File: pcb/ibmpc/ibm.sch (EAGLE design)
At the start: 23 parts, among them J2 ATX24RH

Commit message: working on ibmpc
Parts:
- removed JP3: (no value), appleii:4PIN_FAN
- added JP1: (no value), appleii:4PIN_FAN
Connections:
- net +12V: now also JP1.1_GND; no longer JP3.2_VCC
- net GND: now also JP1.2_VCC; no longer JP3.1_GND
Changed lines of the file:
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@@
 <part name="U$2" library="atx_power_control" deviceset="CAR_FUSE_HOLDER" device="3IN1"/>
 <part name="P+3" library="supply1" library_urn="urn:adsk.eagle:library:371" deviceset="+5V" device=""/>
-<part name="P+5" library="supply1" library_urn="urn:adsk.eagle:library:371" deviceset="+12V" device=""/>
 <part name="J2" library="macse" deviceset="ATX24" device="RH"/>
-<part name="GND4" library="supply1" library_urn="urn:adsk.eagle:library:371" deviceset="GND" device=""/>
-<part name="JP3" library="appleii" deviceset="4PIN_FAN" device=""/>
 <part name="C6" library="clock" deviceset="C-US" device="C1210" value="47uF"/>
 <part name="GND11" library="supply1" library_urn="urn:adsk.eagle:library:371" deviceset="GND" device=""/>
@@
 <part name="C14" library="capacitor-wima" library_urn="urn:adsk.eagle:library:116" deviceset="C" device="5/2.5" package3d_urn="urn:adsk.eagle:package:5426/1"/>
 <part name="GND8" library="supply1" library_urn="urn:adsk.eagle:library:371" deviceset="GND" device=""/>
+<part name="JP1" library="appleii" deviceset="4PIN_FAN" device=""/>
+<part name="GND9" library="supply1" library_urn="urn:adsk.eagle:library:371" deviceset="GND" device=""/>
+<part name="P+7" library="supply1" library_urn="urn:adsk.eagle:library:371" deviceset="+12V" device=""/>
 </parts>
 <sheets>
@@
 <attribute name="VALUE" x="10.16" y="187.96" size="1.778" layer="96" rot="R90"/>
 </instance>
-<instance part="P+5" gate="1" x="-40.64" y="137.16" smashed="yes" rot="MR0">
-<attribute name="VALUE" x="-33.02" y="134.62" size="1.778" layer="96" rot="MR90"/>
-</instance>
 <instance part="J2" gate="G$1" x="96.52" y="175.26" smashed="yes">
 <attribute name="NAME" x="83.82" y="195.58" size="1.27" layer="95"/>
 <attribute name="VALUE" x="83.82" y="149.86" size="1.27" layer="96"/>
 </instance>
-<instance part="GND4" gate="1" x="-86.36" y="137.16" smashed="yes">
-<attribute name="VALUE" x="-88.9" y="134.62" size="1.778" layer="96"/>
-</instance>
-<instance part="JP3" gate="A" x="-55.88" y="132.08" smashed="yes"/>
 <instance part="C6" gate="G$1" x="121.92" y="104.14" smashed="yes">
 <attribute name="NAME" x="122.936" y="104.775" size="1.778" layer="95"/>
@@
 <instance part="GND8" gate="1" x="190.5" y="226.06" smashed="yes">
 <attribute name="VALUE" x="187.96" y="223.52" size="1.778" layer="96"/>
+</instance>
+<instance part="JP1" gate="A" x="256.54" y="226.06" smashed="yes"/>
+<instance part="GND9" gate="1" x="279.4" y="226.06" smashed="yes">
+<attribute name="VALUE" x="276.86" y="223.52" size="1.778" layer="96"/>
+</instance>
+<instance part="P+7" gate="1" x="236.22" y="236.22" smashed="yes" rot="MR0">
+<attribute name="VALUE" x="238.76" y="231.14" size="1.778" layer="96" rot="MR90"/>
 </instance>
 </instances>
@@
 </segment>
 <segment>
-<pinref part="JP3" gate="A" pin="1_GND"/>
-<pinref part="GND4" gate="1" pin="GND"/>
-<wire x1="-68.58" y1="139.7" x2="-86.36" y2="139.7" width="0.1524" layer="91"/>
-</segment>
-<segment>
 <pinref part="C6" gate="G$1" pin="2"/>
 <pinref part="GND11" gate="1" pin="GND"/>
@@
 <pinref part="GND8" gate="1" pin="GND"/>
 </segment>
+<segment>
+<pinref part="JP1" gate="A" pin="2_VCC"/>
+<pinref part="GND9" gate="1" pin="GND"/>
+<wire x1="243.84" y1="228.6" x2="279.4" y2="228.6" width="0.1524" layer="91"/>
+</segment>
 </net>
 <net name="N$6" class="0">
@@
 </segment>
 <segment>
-<pinref part="JP3" gate="A" pin="2_VCC"/>
-<pinref part="P+5" gate="1" pin="+12V"/>
-<wire x1="-68.58" y1="134.62" x2="-40.64" y2="134.62" width="0.1524" layer="91"/>
-</segment>
-<segment>
 <pinref part="C6" gate="G$1" pin="1"/>
 <pinref part="P+8" gate="1" pin="+12V"/>
@@
 <wire x1="114.3" y1="264.16" x2="142.24" y2="264.16" width="0.1524" layer="91"/>
 </segment>
+<segment>
+<pinref part="P+7" gate="1" pin="+12V"/>
+<pinref part="JP1" gate="A" pin="1_GND"/>
+<wire x1="236.22" y1="233.68" x2="243.84" y2="233.68" width="0.1524" layer="91"/>
+</segment>
 </net>

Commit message: ibmpc done
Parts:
- added C15: 100nF, clock:CAP0805
- added JP2: (no value), pinhead:PINHD-1X3
- added JP3: (no value), pinhead:PINHD-1X2
- added LED1: (no value), adafruit:LED5MM
- added R1: (no value), adafruit:R-US_0207/10
- added TP1, TP2: PTR1PAD1-20, testpad:PTR1PAD1-20
- added U$4: ROCKSW, apricot:ROCKSW
- C13: value (none) -> 100nF; device capacitor-wima:C5/2.5 -> clock:CAP0805
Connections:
- new net N$10: JP2.2, U$4.2
- new net N$11: JP2.3, U$4.3
- new net N$12: LED1.C, R1.1
- new net N$9: JP2.1, U$4.1
- net +12V: now also TP1.TP
- net +3V3: now also C13.2, C15.2, LED1.A; no longer C13.1
- net GND: now also C13.1, C15.1, JP3.2, R1.2, TP2.TP, U$4.PEG1, U$4.PEG2; no longer C13.2
- net N$3: now also JP3.1
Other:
- moved on the sheet: C13

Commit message: cleanup
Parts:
- added U$7: M3_MOUNTING_HOLE, apricot:M3_MOUNTING_HOLE
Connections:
- net GND: now also U$7.P$1, U$7.P$2
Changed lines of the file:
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@@
 <part name="GND13" library="supply1" library_urn="urn:adsk.eagle:library:371" deviceset="GND" device=""/>
 <part name="P+5" library="supply1" library_urn="urn:adsk.eagle:library:371" deviceset="+12V" device=""/>
+<part name="U$7" library="apricot" deviceset="M3_MOUNTING_HOLE" device=""/>
+<part name="GND14" library="supply1" library_urn="urn:adsk.eagle:library:371" deviceset="GND" device=""/>
 </parts>
 <sheets>
@@
 <instance part="P+5" gate="1" x="30.48" y="114.3" smashed="yes" rot="MR0">
 <attribute name="VALUE" x="33.02" y="109.22" size="1.778" layer="96" rot="MR90"/>
+</instance>
+<instance part="U$7" gate="G$1" x="-35.56" y="139.7" smashed="yes"/>
+<instance part="GND14" gate="1" x="-7.62" y="134.62" smashed="yes">
+<attribute name="VALUE" x="-10.16" y="132.08" size="1.778" layer="96"/>
 </instance>
 </instances>
@@
 <pinref part="GND13" gate="1" pin="GND"/>
 </segment>
+<segment>
+<pinref part="GND14" gate="1" pin="GND"/>
+<wire x1="-7.62" y1="144.78" x2="-7.62" y2="137.16" width="0.1524" layer="91"/>
+<pinref part="U$7" gate="G$1" pin="P$1"/>
+<wire x1="-12.7" y1="144.78" x2="-7.62" y2="144.78" width="0.1524" layer="91"/>
+<pinref part="U$7" gate="G$1" pin="P$2"/>
+<wire x1="-12.7" y1="137.16" x2="-7.62" y2="137.16" width="0.1524" layer="91"/>
+<junction x="-7.62" y="137.16"/>
+</segment>
 </net>

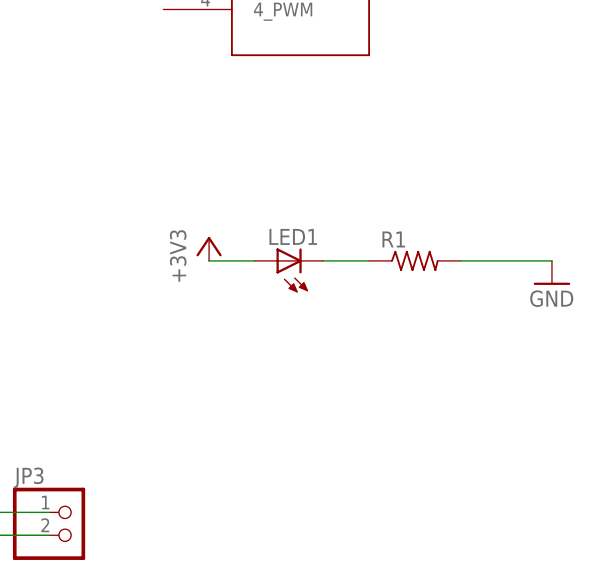
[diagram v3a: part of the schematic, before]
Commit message: updated silkscreen
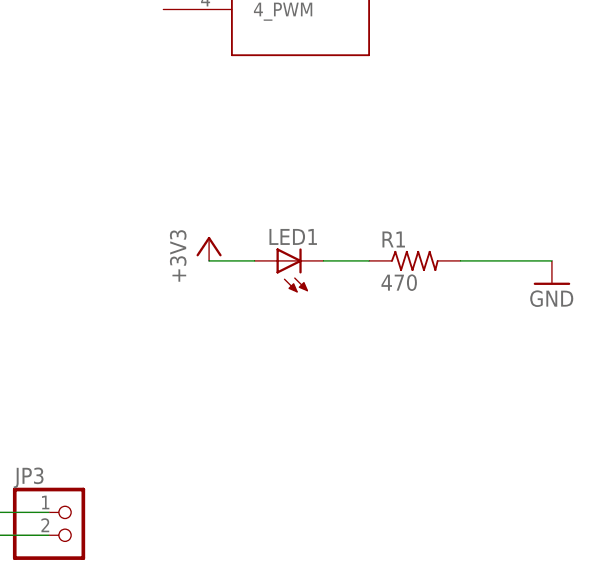
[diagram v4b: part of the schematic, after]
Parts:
- R1: value (none) -> 470
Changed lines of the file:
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@@
 <part name="LED1" library="adafruit" deviceset="LED" device="5MM"/>
 <part name="+3V4" library="supply1" library_urn="urn:adsk.eagle:library:371" deviceset="+3V3" device=""/>
-<part name="R1" library="adafruit" deviceset="R-US_" device="0207/10"/>
+<part name="R1" library="adafruit" deviceset="R-US_" device="0207/10" value="470"/>
 <part name="GND12" library="supply1" library_urn="urn:adsk.eagle:library:371" deviceset="GND" device=""/>
 <part name="TP1" library="testpad" library_urn="urn:adsk.eagle:library:385" deviceset="PTR1" device="PAD1-20" package3d_urn="urn:adsk.eagle:package:27950/1"/>

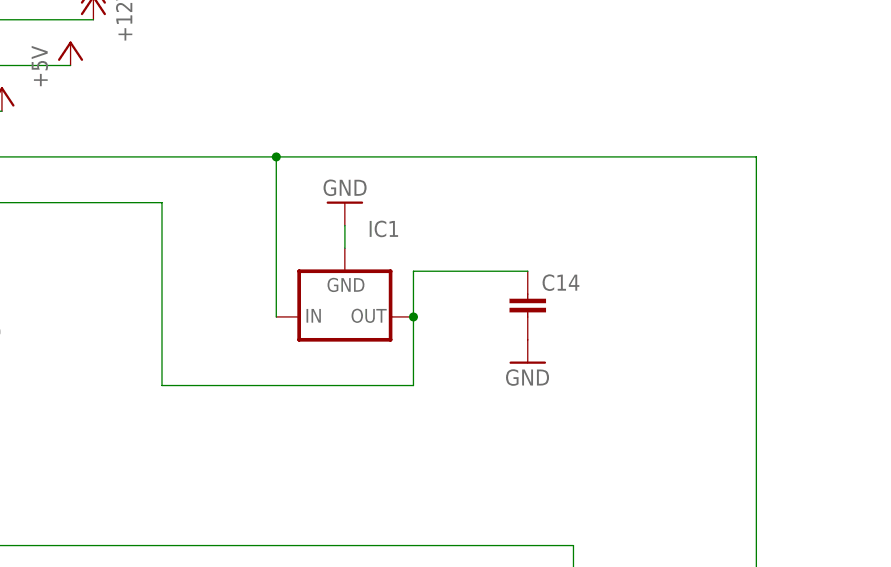
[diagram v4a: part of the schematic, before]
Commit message: changed to 70L05
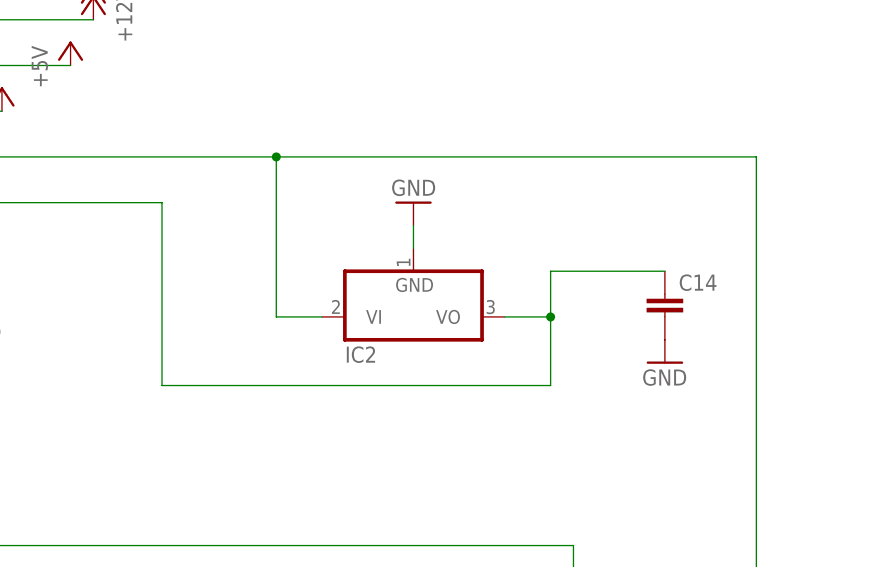
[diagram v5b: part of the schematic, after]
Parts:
- removed IC1: (no value), v-reg:79XXS
- added IC2: (no value), linear:7905L
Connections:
- net GND: now also IC2.GND; no longer IC1.GND
- net N$2: now also IC2.VI; no longer IC1.IN
- net N$7: now also IC2.VO; no longer IC1.OUT
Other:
- moved on the sheet: C14
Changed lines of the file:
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@@
 <part name="P+6" library="supply1" library_urn="urn:adsk.eagle:library:371" deviceset="+12V" device=""/>
 <part name="+3V3" library="supply1" library_urn="urn:adsk.eagle:library:371" deviceset="+3V3" device=""/>
-<part name="IC1" library="v-reg" library_urn="urn:adsk.eagle:library:409" deviceset="79XXS" device="" package3d_urn="urn:adsk.eagle:package:30343/1"/>
 <part name="GND7" library="supply1" library_urn="urn:adsk.eagle:library:371" deviceset="GND" device=""/>
 <part name="C14" library="capacitor-wima" library_urn="urn:adsk.eagle:library:116" deviceset="C" device="5/2.5" package3d_urn="urn:adsk.eagle:package:5426/1"/>
@@
 <part name="U$7" library="apricot" deviceset="M3_MOUNTING_HOLE" device=""/>
 <part name="GND14" library="supply1" library_urn="urn:adsk.eagle:library:371" deviceset="GND" device=""/>
+<part name="IC2" library="linear" library_urn="urn:adsk.eagle:library:262" deviceset="79*" device="L" package3d_urn="urn:adsk.eagle:package:16416/2" technology="05"/>
 </parts>
 <sheets>
@@
 <attribute name="VALUE" x="129.54" y="251.46" size="1.778" layer="96" rot="R90"/>
 </instance>
-<instance part="IC1" gate="1" x="170.18" y="231.14" smashed="yes">
-<attribute name="NAME" x="172.72" y="240.03" size="1.778" layer="95"/>
-<attribute name="VALUE" x="172.72" y="237.49" size="1.778" layer="96"/>
-</instance>
-<instance part="GND7" gate="1" x="170.18" y="243.84" smashed="yes" rot="R180">
-<attribute name="VALUE" x="172.72" y="246.38" size="1.778" layer="96" rot="R180"/>
-</instance>
-<instance part="C14" gate="G$1" x="190.5" y="233.68" smashed="yes">
-<attribute name="NAME" x="192.024" y="234.061" size="1.778" layer="95"/>
-<attribute name="VALUE" x="192.024" y="228.981" size="1.778" layer="96"/>
-</instance>
-<instance part="GND8" gate="1" x="190.5" y="226.06" smashed="yes">
-<attribute name="VALUE" x="187.96" y="223.52" size="1.778" layer="96"/>
+<instance part="GND7" gate="1" x="177.8" y="243.84" smashed="yes" rot="R180">
+<attribute name="VALUE" x="180.34" y="246.38" size="1.778" layer="96" rot="R180"/>
+</instance>
+<instance part="C14" gate="G$1" x="205.74" y="233.68" smashed="yes">
+<attribute name="NAME" x="207.264" y="234.061" size="1.778" layer="95"/>
+<attribute name="VALUE" x="207.264" y="228.981" size="1.778" layer="96"/>
+</instance>
+<instance part="GND8" gate="1" x="205.74" y="226.06" smashed="yes">
+<attribute name="VALUE" x="203.2" y="223.52" size="1.778" layer="96"/>
 </instance>
 <instance part="JP1" gate="A" x="256.54" y="226.06" smashed="yes"/>
@@
 <instance part="GND14" gate="1" x="-7.62" y="134.62" smashed="yes">
 <attribute name="VALUE" x="-10.16" y="132.08" size="1.778" layer="96"/>
+</instance>
+<instance part="IC2" gate="A1" x="177.8" y="233.68" smashed="yes">
+<attribute name="NAME" x="170.18" y="226.06" size="1.778" layer="95"/>
+<attribute name="VALUE" x="170.18" y="223.52" size="1.778" layer="96"/>
 </instance>
 </instances>
@@
 </segment>
 <segment>
-<pinref part="IC1" gate="1" pin="GND"/>
-<pinref part="GND7" gate="1" pin="GND"/>
-<wire x1="170.18" y1="238.76" x2="170.18" y2="241.3" width="0.1524" layer="91"/>
-</segment>
-<segment>
 <pinref part="C14" gate="G$1" pin="2"/>
 <pinref part="GND8" gate="1" pin="GND"/>
@@
 <wire x1="-12.7" y1="137.16" x2="-7.62" y2="137.16" width="0.1524" layer="91"/>
 <junction x="-7.62" y="137.16"/>
+</segment>
+<segment>
+<pinref part="GND7" gate="1" pin="GND"/>
+<pinref part="IC2" gate="A1" pin="GND"/>
+<wire x1="177.8" y1="241.3" x2="177.8" y2="238.76" width="0.1524" layer="91"/>
 </segment>
 </net>
@@
 <pinref part="U$1" gate="G$1" pin="-12V"/>
 <wire x1="215.9" y1="248.92" x2="162.56" y2="248.92" width="0.1524" layer="91"/>
-<pinref part="IC1" gate="1" pin="IN"/>
 <wire x1="162.56" y1="248.92" x2="114.3" y2="248.92" width="0.1524" layer="91"/>
 <wire x1="162.56" y1="231.14" x2="162.56" y2="248.92" width="0.1524" layer="91"/>
 <junction x="162.56" y="248.92"/>
+<pinref part="IC2" gate="A1" pin="VI"/>
+<wire x1="162.56" y1="231.14" x2="167.64" y2="231.14" width="0.1524" layer="91"/>
 </segment>
 </net>
@@
 <net name="N$7" class="0">
 <segment>
-<pinref part="IC1" gate="1" pin="OUT"/>
-<wire x1="177.8" y1="231.14" x2="177.8" y2="223.52" width="0.1524" layer="91"/>
-<wire x1="177.8" y1="223.52" x2="149.86" y2="223.52" width="0.1524" layer="91"/>
+<wire x1="193.04" y1="223.52" x2="149.86" y2="223.52" width="0.1524" layer="91"/>
 <wire x1="149.86" y1="223.52" x2="149.86" y2="243.84" width="0.1524" layer="91"/>
 <wire x1="149.86" y1="243.84" x2="114.3" y2="243.84" width="0.1524" layer="91"/>
 <pinref part="U$1" gate="G$1" pin="-5V"/>
 <pinref part="C14" gate="G$1" pin="1"/>
-<wire x1="177.8" y1="231.14" x2="177.8" y2="236.22" width="0.1524" layer="91"/>
-<wire x1="177.8" y1="236.22" x2="190.5" y2="236.22" width="0.1524" layer="91"/>
-<junction x="177.8" y="231.14"/>
-</segment>
-</net>
+<wire x1="193.04" y1="236.22" x2="205.74" y2="236.22" width="0.1524" layer="91"/>
+<pinref part="IC2" gate="A1" pin="VO"/>
+<wire x1="187.96" y1="231.14" x2="193.04" y2="231.14" width="0.1524" layer="91"/>
+<wire x1="193.04" y1="231.14" x2="193.04" y2="236.22" width="0.1524" layer="91"/>
+<wire x1="193.04" y1="223.52" x2="193.04" y2="231.14" width="0.1524" layer="91"/>
+<junction x="193.04" y="231.14"/>
+</segment>
+</net>

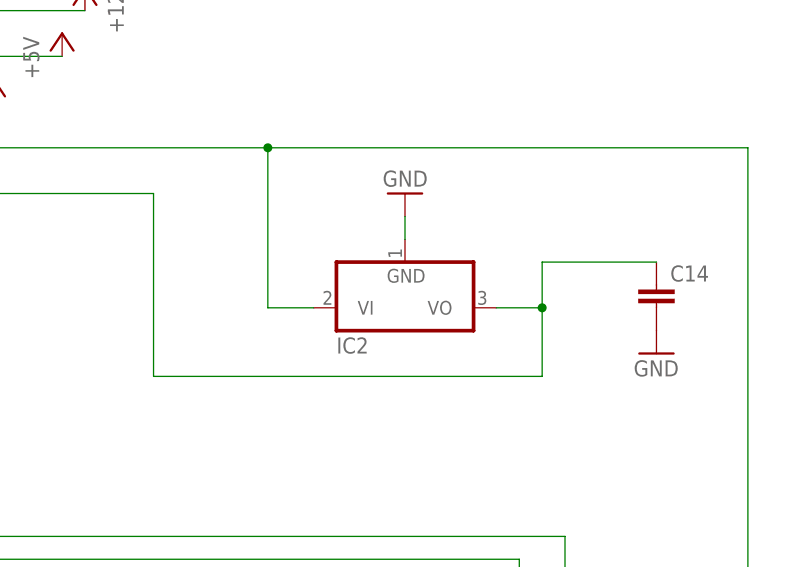
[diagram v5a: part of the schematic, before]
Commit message: switched back to 7905
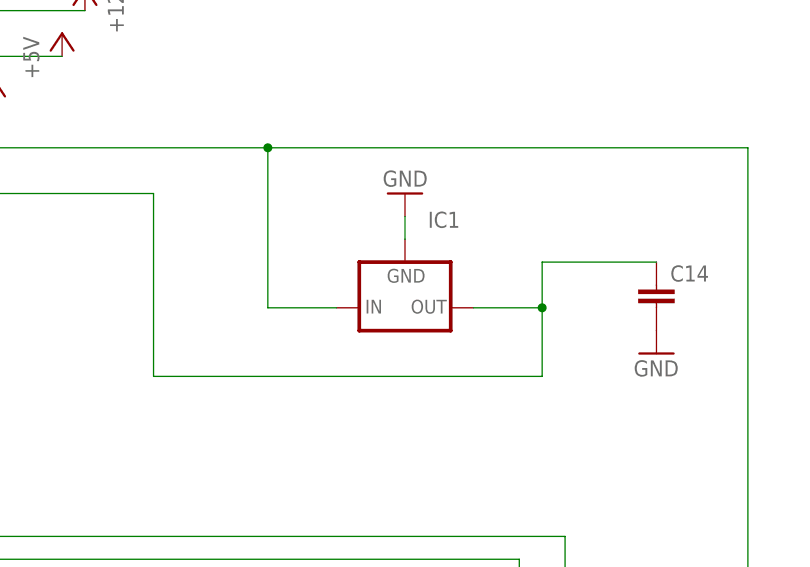
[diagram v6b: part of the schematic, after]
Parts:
- removed IC2: (no value), linear:7905L
- added IC1: (no value), v-reg:79XXS
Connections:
- net GND: now also IC1.GND; no longer IC2.GND
- net N$2: now also IC1.IN; no longer IC2.VI
- net N$7: now also IC1.OUT; no longer IC2.VO
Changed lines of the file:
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@@
 <part name="U$7" library="apricot" deviceset="M3_MOUNTING_HOLE" device=""/>
 <part name="GND14" library="supply1" library_urn="urn:adsk.eagle:library:371" deviceset="GND" device=""/>
-<part name="IC2" library="linear" library_urn="urn:adsk.eagle:library:262" deviceset="79*" device="L" package3d_urn="urn:adsk.eagle:package:16416/2" technology="05"/>
+<part name="IC1" library="v-reg" library_urn="urn:adsk.eagle:library:409" deviceset="79XXS" device="" package3d_urn="urn:adsk.eagle:package:30343/1"/>
 </parts>
 <sheets>
@@
 <attribute name="VALUE" x="-10.16" y="132.08" size="1.778" layer="96"/>
 </instance>
-<instance part="IC2" gate="A1" x="177.8" y="233.68" smashed="yes">
-<attribute name="NAME" x="170.18" y="226.06" size="1.778" layer="95"/>
-<attribute name="VALUE" x="170.18" y="223.52" size="1.778" layer="96"/>
+<instance part="IC1" gate="1" x="177.8" y="231.14" smashed="yes">
+<attribute name="NAME" x="180.34" y="240.03" size="1.778" layer="95"/>
+<attribute name="VALUE" x="180.34" y="237.49" size="1.778" layer="96"/>
 </instance>
 </instances>
@@
 <segment>
 <pinref part="GND7" gate="1" pin="GND"/>
-<pinref part="IC2" gate="A1" pin="GND"/>
 <wire x1="177.8" y1="241.3" x2="177.8" y2="238.76" width="0.1524" layer="91"/>
+<pinref part="IC1" gate="1" pin="GND"/>
 </segment>
 </net>
@@
 <wire x1="162.56" y1="231.14" x2="162.56" y2="248.92" width="0.1524" layer="91"/>
 <junction x="162.56" y="248.92"/>
-<pinref part="IC2" gate="A1" pin="VI"/>
-<wire x1="162.56" y1="231.14" x2="167.64" y2="231.14" width="0.1524" layer="91"/>
+<wire x1="162.56" y1="231.14" x2="170.18" y2="231.14" width="0.1524" layer="91"/>
+<pinref part="IC1" gate="1" pin="IN"/>
 </segment>
 </net>
@@
 <pinref part="C14" gate="G$1" pin="1"/>
 <wire x1="193.04" y1="236.22" x2="205.74" y2="236.22" width="0.1524" layer="91"/>
-<pinref part="IC2" gate="A1" pin="VO"/>
-<wire x1="187.96" y1="231.14" x2="193.04" y2="231.14" width="0.1524" layer="91"/>
+<wire x1="185.42" y1="231.14" x2="193.04" y2="231.14" width="0.1524" layer="91"/>
 <wire x1="193.04" y1="231.14" x2="193.04" y2="236.22" width="0.1524" layer="91"/>
 <wire x1="193.04" y1="223.52" x2="193.04" y2="231.14" width="0.1524" layer="91"/>
 <junction x="193.04" y="231.14"/>
-</segment>
-</net>
+<pinref part="IC1" gate="1" pin="OUT"/>
+</segment>
+</net>
